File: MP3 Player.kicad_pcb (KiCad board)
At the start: 2 copper layers, 67.3 x 67.8 mm, 48 parts, among them J1 Conn_01x02_Pin, J2 USB_C_Receptacle_USB2.0_14P, J3 SJ2-3574A-SMT-TR, J4 Conn_01x02_Pin, J5 1051620001, J6 Conn_01x04_Pin, Q1 IRLML6402, SW1 SW_SPDT, SW2 SW_MEC_5E, SW3 SW_MEC_5E, SW4 SW_MEC_5E, SW5 SW_MEC_5E, SW6 SW_MEC_5E, SW7 SW_MEC_5E, SW8 SW_MEC_5E, U1 ESP32-S3-WROOM-1U-N16R8, U2 TLV1117-33, U3 TLV320DAC3100IRHBR, U5 AP2127K-1.8TRG1

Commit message: updated board design
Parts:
- added C10: 10uF, Capacitor_SMD:C_0805_2012Metric, F.Cu at (164.3, 75.0)
- added C11: 10uF, Capacitor_SMD:C_0805_2012Metric, F.Cu at (143.7, 99.2)
- added C3: 10uF, Capacitor_SMD:C_0805_2012Metric, F.Cu at (164.3, 69.0)
- added C4: 10uF, Capacitor_SMD:C_0805_2012Metric, F.Cu at (164.3, 72.0)
- added D1: LED, LED_SMD:LED_0603_1608Metric_Pad1.05x0.95mm_HandSolder, F.Cu at (153.2, 94.9)
- added R1: 470, Resistor_SMD:R_0805_2012Metric, F.Cu at (153.2, 92.2)
- added R3: 5k1, Resistor_SMD:R_0805_2012Metric, F.Cu at (164.3, 78.0)
- added R9: 5k1, Resistor_SMD:R_0805_2012Metric, F.Cu at (164.3, 81.0)
- U1: footprint ESP32_S3_WROOM_1U_N16R8:XCVR_ESP32-S3-WROOM-1U-N16R8 -> RF_Module:ESP32-S3-WROOM-1U
- U3: footprint TLV320DAC3100IRHBR:IC_ADS125H01IRHBT -> TLV320DAC3100:IC_ADS125H01IRHBT
- moved U1 0.09 mm to (216.5, 83.8)
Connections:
- C12 pad 1: +3V3 -> GND
- C12 pad 2: GND -> +3V3
- C7 pad 1: /HPL -> Net-(C7-Pad1)
- C8 pad 1: /HRP -> Net-(C8-Pad1)
- J3 pad 2: /HPL -> Net-(C7-Pad1)
- J3 pad 3: /HRP -> Net-(C8-Pad1)
- J5 pad G1: Net-(J5-GND-PadG1) -> GND
- J5 pad G2: Net-(J5-GND-PadG1) -> GND
- J5 pad G3: Net-(J5-GND-PadG1) -> GND
- J5 pad G4: Net-(J5-GND-PadG1) -> GND
- Q1 pad 3: /vbat -> /vin
- SW1 pad 2: /vbat -> /vin
- U1 pad 12: /MISO -> /ESP32-S3/MISO
- U1 pad 17: /MOSI -> /ESP32-S3/MOSI
- U1 pad 18: /SCLK -> /ESP32-S3/SCLK
- U1 pad 19: /DET -> /ESP32-S3/DET
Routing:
- net Net-(J5-GND-PadG1): track 16.7 -> 0.00 mm
- net /HRP: track 20.7 -> 12.3 mm
- net /HPL: track 20.3 -> 11.9 mm
- net /SPKP: track 26.2 -> 34.1 mm, vias 1 -> 3
- net +3V3: track 59.0 -> 63.8 mm, vias 30 -> 29
- net Net-(C8-Pad1): track 0.00 -> 4.51 mm
- net Net-(C7-Pad1): track 0.00 -> 4.42 mm
- net /SPKM: track 35.6 -> 38.7 mm
- net GND: track 55.7 -> 58.7 mm, vias 32 -> 30
- net /SCL: track 78.0 -> 76.3 mm
- net /RES: track 63.9 -> 62.8 mm

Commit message: updated board design
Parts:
- removed the C10 at (197.7, 73.4)
- removed the C11 at (245.6, 86.6)
- removed the C3 at (192.9, 77.0)
- removed the C4 at (231.1, 94.0)
- removed the D1 at (201.7, 84.8)
- removed the R1 at (200.7, 88.1)
- removed the R3 at (192.9, 72.9)
- removed the R9 at (231.1, 89.8)
- moved C8 70.6 mm to (172.0, 95.0), turned to 90 degrees
- moved C1 70.1 mm to (122.1, 80.0)
- moved C2 70.1 mm to (122.5, 68.6)
- moved J2 70.1 mm to (114.6, 90.3)
- moved MCP73831 70.1 mm to (124.7, 84.0)
- moved R12 70.1 mm to (126.9, 123.3)
- moved R2 70.1 mm to (127.8, 83.3)
- moved R5 70.1 mm to (126.9, 91.9)
- moved SW8 70.1 mm to (122.5, 101.1)
- moved C12 70.1 mm to (152.9, 103.1)
- moved C5 70.1 mm to (165.9, 74.4)
- moved C6 70.1 mm to (169.7, 73.1)
- moved C7 70.1 mm to (168.2, 95.0), turned to 90 degrees
- moved C9 70.1 mm to (120.5, 84.3)
- moved D2 70.1 mm to (125.6, 78.2)
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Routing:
- net /vbat: track 61.5 -> 40.7 mm
- net /vin: track 0.00 -> 18.6 mm
- net +3V3: track 63.8 -> 73.4 mm, vias 29 -> 33
- net Net-(C8-Pad1): track 4.51 -> 12.1 mm
- net Net-(C7-Pad1): track 4.42 -> 11.9 mm
- net /HRP: track 12.3 -> 8.16 mm
- net /HPL: track 11.9 -> 8.29 mm
- net /SCL: track 76.3 -> 78.0 mm
- net /BOOT: track 43.0 -> 44.4 mm
- net /RES: track 62.8 -> 63.9 mm

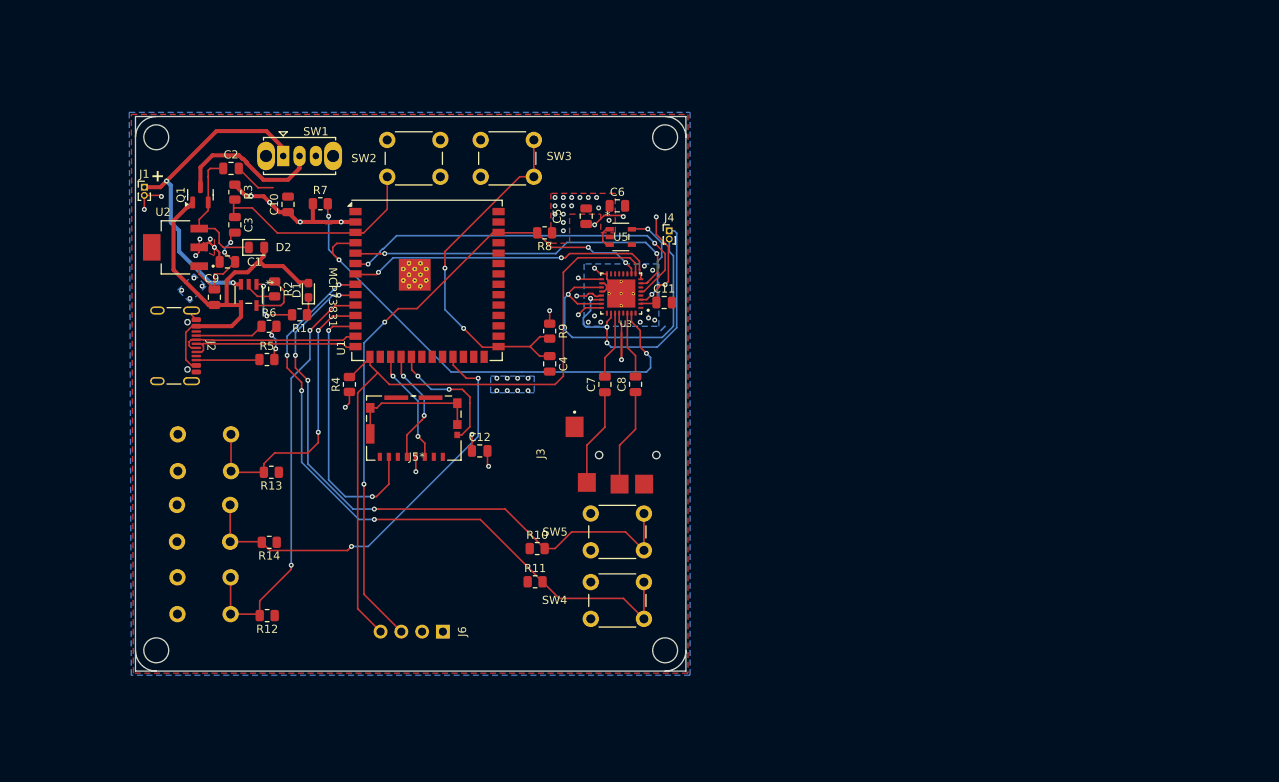
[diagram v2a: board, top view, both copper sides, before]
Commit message: updated board design to fit altoid tin
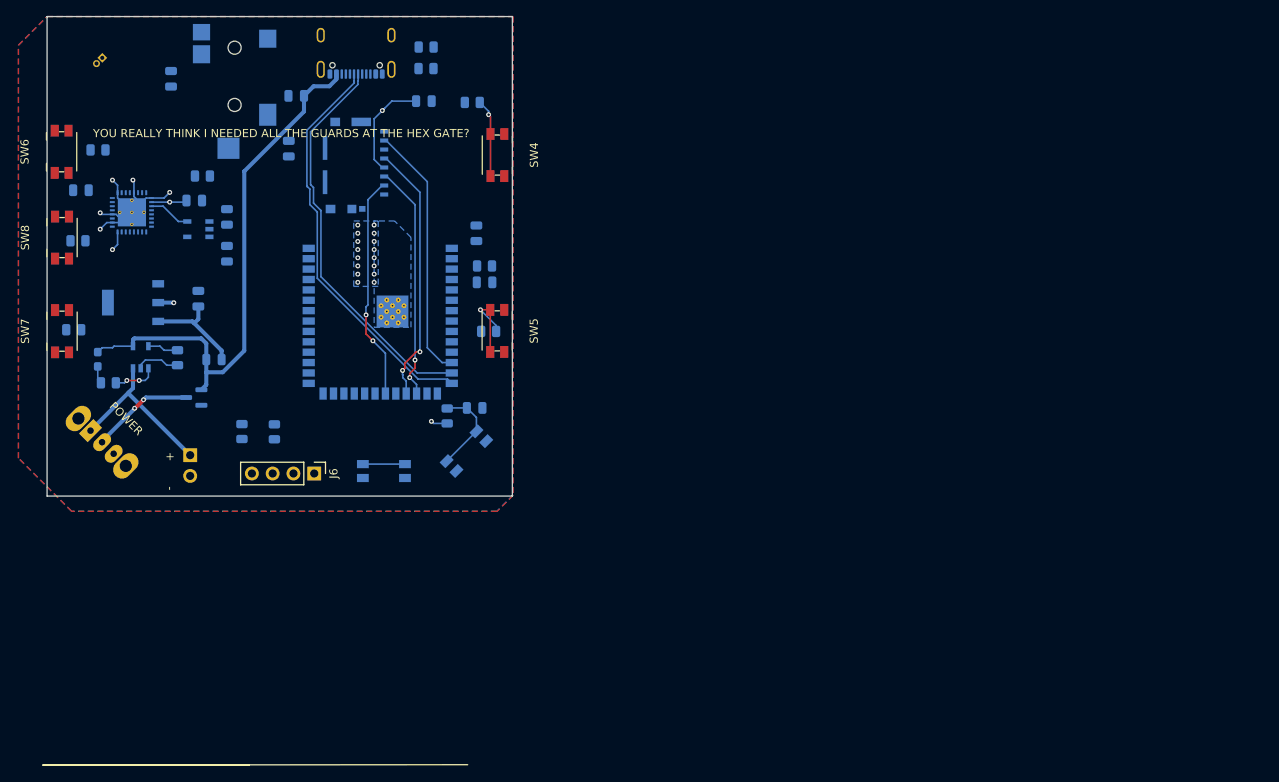
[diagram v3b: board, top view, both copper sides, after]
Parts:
- removed SW2, SW3: SW_MEC_5E, Button_Switch_THT:SW_PUSH_6mm
- added SW10: SW_MEC_5E, Button_Switch_SMD:Panasonic_EVQPUK_EVQPUB, B.Cu at (151.3, 103.1)
- added SW9: SW_MEC_5E, Button_Switch_SMD:Panasonic_EVQPUK_EVQPUB, B.Cu at (141.2, 105.6)
- C1, C10, C11, C12, C2, C3, C4, C5, C6, C7, C8, C9, D1, D2, J2, J4, Q1, R1, R10, R11, R12, R13, R14, R2, R3, R4, R5, R6, R7, R8, R9, SW1, U1, U3: moved to B.Cu
- J1: footprint Connector_PinHeader_1.00mm:PinHeader_1x02_P1.00mm_Vertical -> Connector_PinHeader_2.54mm:PinHeader_1x02_P2.54mm_Vertical; moved to B.Cu
- J3: footprint SJ2_3574A_SMT_TR:SAMESKY_SJ2-3574A-SMT-TR -> 35RASMT4BHNTRX:35RASMT4BHNTRX_SWC; moved to B.Cu
- J5: footprint SD CARD READER:105162-0001_MOL -> 35RASMT4BHNTRX:105162-0001_MOL; moved to B.Cu
- J6: moved to F.Cu
- MCP73831: footprint MCP73831:SOT-23-5_MC_MCH -> footprints:SOT-23-5_AP2127K_DIO; moved to B.Cu
- SW4, SW5: footprint Button_Switch_THT:SW_PUSH_6mm -> Button_Switch_SMD:Panasonic_EVQPUK_EVQPUB
- SW6, SW7, SW8: footprint Button_Switch_THT:SW_PUSH_6mm -> Button_Switch_SMD:Panasonic_EVQPUK_EVQPUB; moved to F.Cu
- U2: footprint TLV1117LV33DCYR:VREG_TLV1117LV33DCYR -> TLV1117:DCY0004A_L; moved to B.Cu
- U5: footprint AP2127K_1_8TRG1:SOT-23-5_AP2127K_DIO -> footprints:SOT-23-5_AP2127K_DIO; moved to B.Cu
- moved J4 72.5 mm to (106.8, 55.0), turned to 135 degrees
- moved J3 65.9 mm to (122.9, 58.6), turned to 180 degrees
- moved C7 64.9 mm to (115.2, 57.6), turned to -90 degrees
- moved U3 60.7 mm to (110.4, 73.9)
- moved R12 60.6 mm to (106.2, 66.3)
- moved R11 59.1 mm to (152.0, 60.5)
- moved C11 58.8 mm to (118.0, 72.5)
- moved SW6 56.0 mm to (101.8, 66.5), turned to 90 degrees
- moved SW4 53.5 mm to (155.1, 66.9), turned to -90 degrees
- moved U5 51.7 mm to (118.5, 76.0), turned to 180 degrees
- moved C8 51.3 mm to (129.6, 66.2), turned to -90 degrees
- moved C6 48.1 mm to (122.0, 79.0), turned to -90 degrees
- moved C5 43.9 mm to (122.0, 74.5)
- moved R14 43.7 mm to (103.8, 77.4)
- moved J2 43.6 mm to (137.8, 53.4), turned to 0 degrees
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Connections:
- net /D_N renamed /USB_N
- net /D_P renamed /USB_P
- SW4 pad 1: /vol+ -> +3V3
- SW5 pad 1: /vol- -> +3V3
- SW6 pad 1: /up -> +3V3
- SW7 pad 1: /sel -> +3V3
- SW7 pad 2: /sel -> /down
- SW8 pad 1: /down -> +3V3
- SW8 pad 2: /down -> /sel
- U1 pad 12: /ESP32-S3/MISO -> /MISO
- U1 pad 17: /ESP32-S3/MOSI -> /MOSI
- U1 pad 18: /ESP32-S3/SCLK -> /SCLK
- U1 pad 20: unconnected-(U1-IO12-Pad20) -> /CS
- U1 pad 41: GND -> (no net)
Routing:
- net /SDA: track 87.2 -> 0.00 mm
- net /SCL: track 78.0 -> 0.00 mm, vias 4 -> 0
- net /vol+: track 81.5 -> 9.55 mm, vias 4 -> 1
- net /vol-: track 77.6 -> 9.78 mm, vias 4 -> 1
- net /RES: track 63.9 -> 0.00 mm, vias 3 -> 0
- net /sel: track 52.8 -> 0.00 mm, vias 2 -> 0
- net /up: track 52.4 -> 0.00 mm, vias 2 -> 0
- net +3V3: track 73.4 -> 21.3 mm, vias 33 -> 12
- net /DIN: track 46.3 -> 0.00 mm, vias 2 -> 0
- net /BCLK: track 43.1 -> 0.00 mm, vias 2 -> 0
- net /SPKM: track 38.7 -> 0.00 mm, vias 1 -> 0
- net /MCLK: track 38.4 -> 0.00 mm, vias 2 -> 0
- net /down: track 36.4 -> 0.00 mm, vias 2 -> 0
- net GND: track 58.7 -> 23.8 mm, vias 30 -> 14
- net /SPKP: track 34.1 -> 0.00 mm, vias 3 -> 0
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- removed copper zone on B.Cu, net +3V3
- removed copper zone on F.Cu, net GND
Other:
- board size 67.3 x 67.8 mm -> 56.9 x 58.6 mm
- board text added: "+ -"
- board text added: "POWER"
- board text added: "YOU REALLY THINK I NEEDED ALL THE GUARDS AT THE HEX GATE?"
- board text removed: "+"
